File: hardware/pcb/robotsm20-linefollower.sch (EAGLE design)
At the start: 132 parts, among them Q5 BSS138LT3G, Q6 BSS138LT3G, Q7 BSS138LT3G, Q8 BSS138LT3G, U1 STM32F405RG

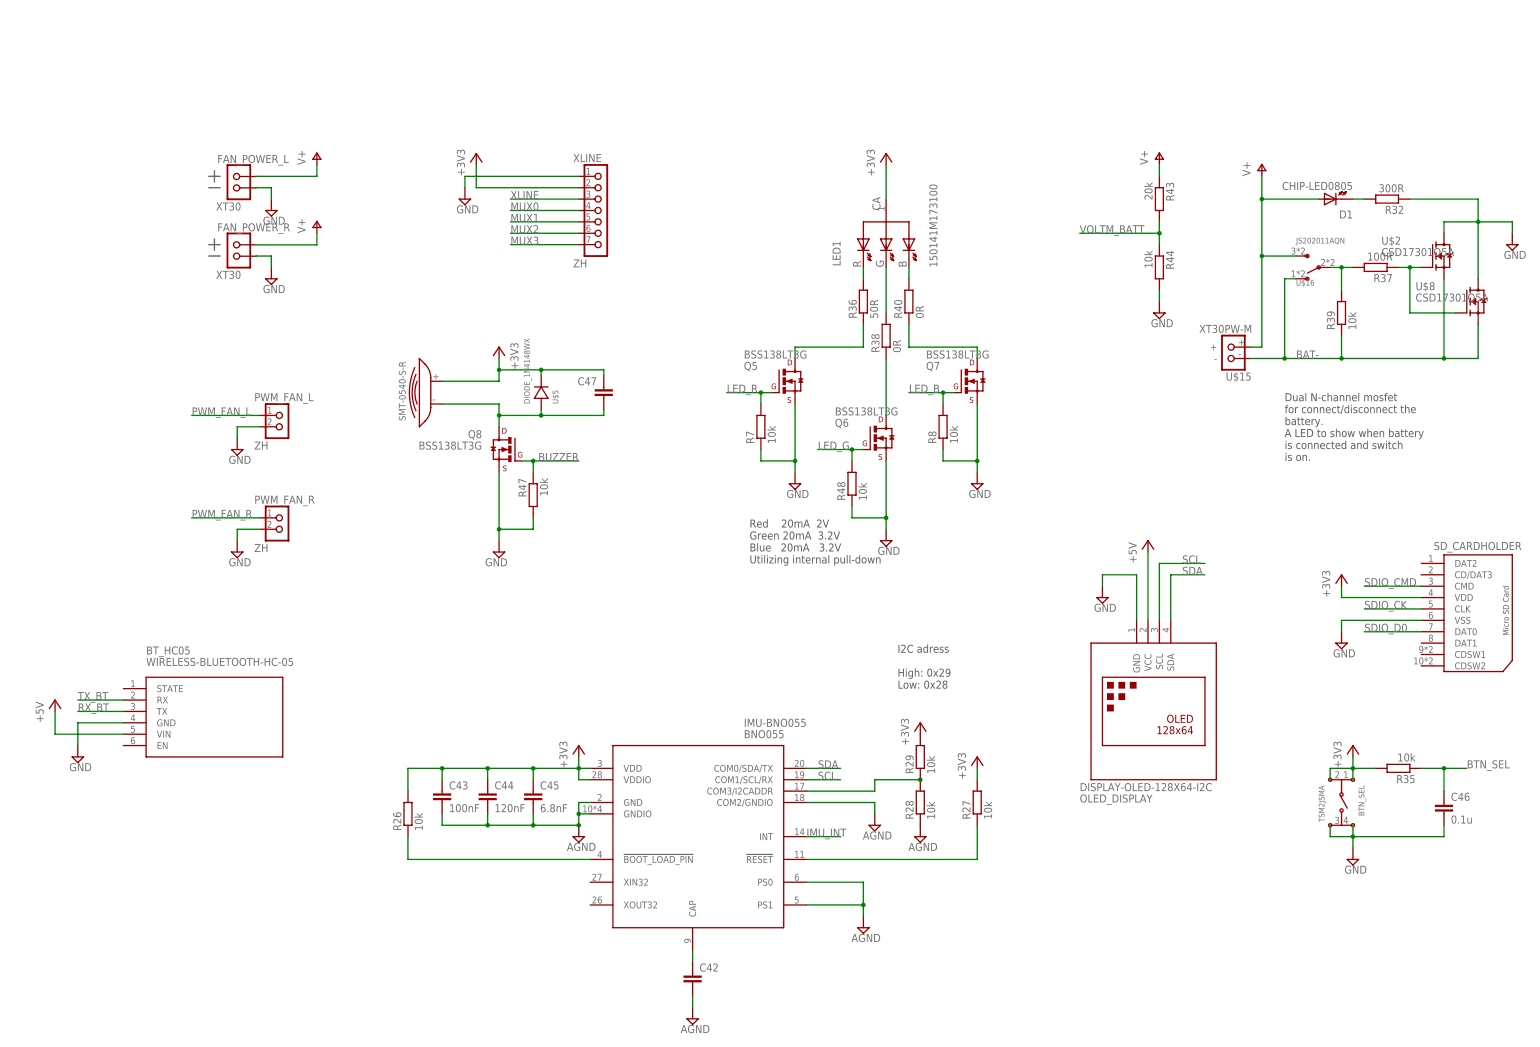
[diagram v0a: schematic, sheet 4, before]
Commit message: Motor mounts added
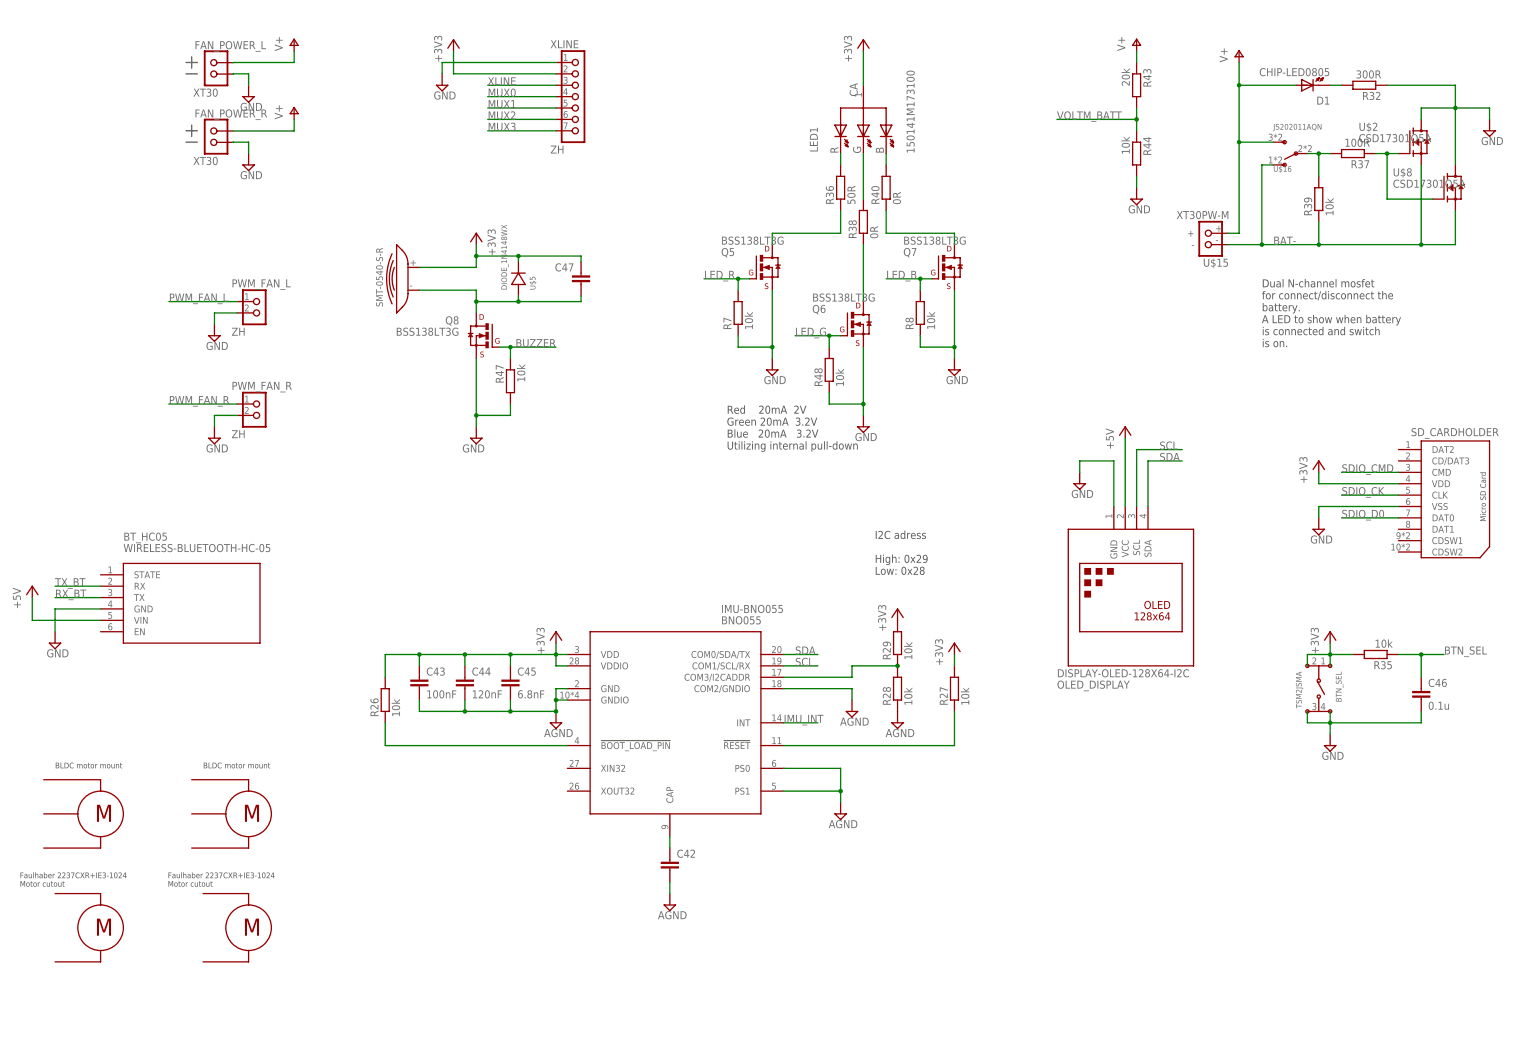
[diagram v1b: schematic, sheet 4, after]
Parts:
- added U$11, U$12: FAULHABER-2237CXR+IE3-1024, MISC:FAULHABER-2237CXR+IE3-1024
- added U$6, U$7: EMAX-1306/1606_MOTOR_MOUNT, MISC:EMAX-1306/1606_MOTOR_MOUNT
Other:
- moved on the sheet: BTN_SEL, BT_HC05, C42, C43, C44, C45, C46, C47, D1, FAN_POWER_L, FAN_POWER_R, IMU-BNO055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

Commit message: Correction work
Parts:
- removed C41: 270pF, rcl:C-EUC0805
- removed R16, R21: (no value), rcl:R-EU_R0603
- added COSC: 270pF, rcl:C-EUC0805
- added CVCC: 0.1µF, rcl:C-EUC0805
- added ROSC: 3.14k, rcl:R-EU_R0603
- added TP1, TP2: TEST-POINT3X5, Isaks Bibliotek:TEST-POINT3X5
- ENC_L, ENC_R: value ZR_B6B-ZR -> ZH-6
- MOTOR_L, MOTOR_R: value EH_B2B-EH -> EH-2
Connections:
- removed net N$24: BOOST.EN, R16.1
- removed net N$29: C41.1, MOTORDRIVER.VCC, R21.2, R23.2
- removed net N$9: C3.1, CURRENTAMP.VS
- new net VCC5V: CVCC.1, MOTORDRIVER.TBLKAB, MOTORDRIVER.VCC, R1.2, R2.2, R23.2, ROSC.2
- net +3V3: now also C3.1, CURRENTAMP.VS; no longer R1.2, R2.2
- net GND: now also COSC.2, CVCC.2; no longer C41.2
- net LO1: now also TP2.1
- net LO2: now also TP1.1
- net N$31: now also COSC.1, ROSC.1; no longer R21.1
- net V+: no longer R16.2
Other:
- note added: "Float to enable IC"
- note added: "Vref for constant current mode Iout = Vref * 2.5"
- note added: "fchop = 1/4 Rosc^(-0.8) f in MHz, R in Kohm 1.8kohm for 150kHz 3.14ohm for 100kHz 8.2kohm for 50kHz"
- moved on the sheet: R3

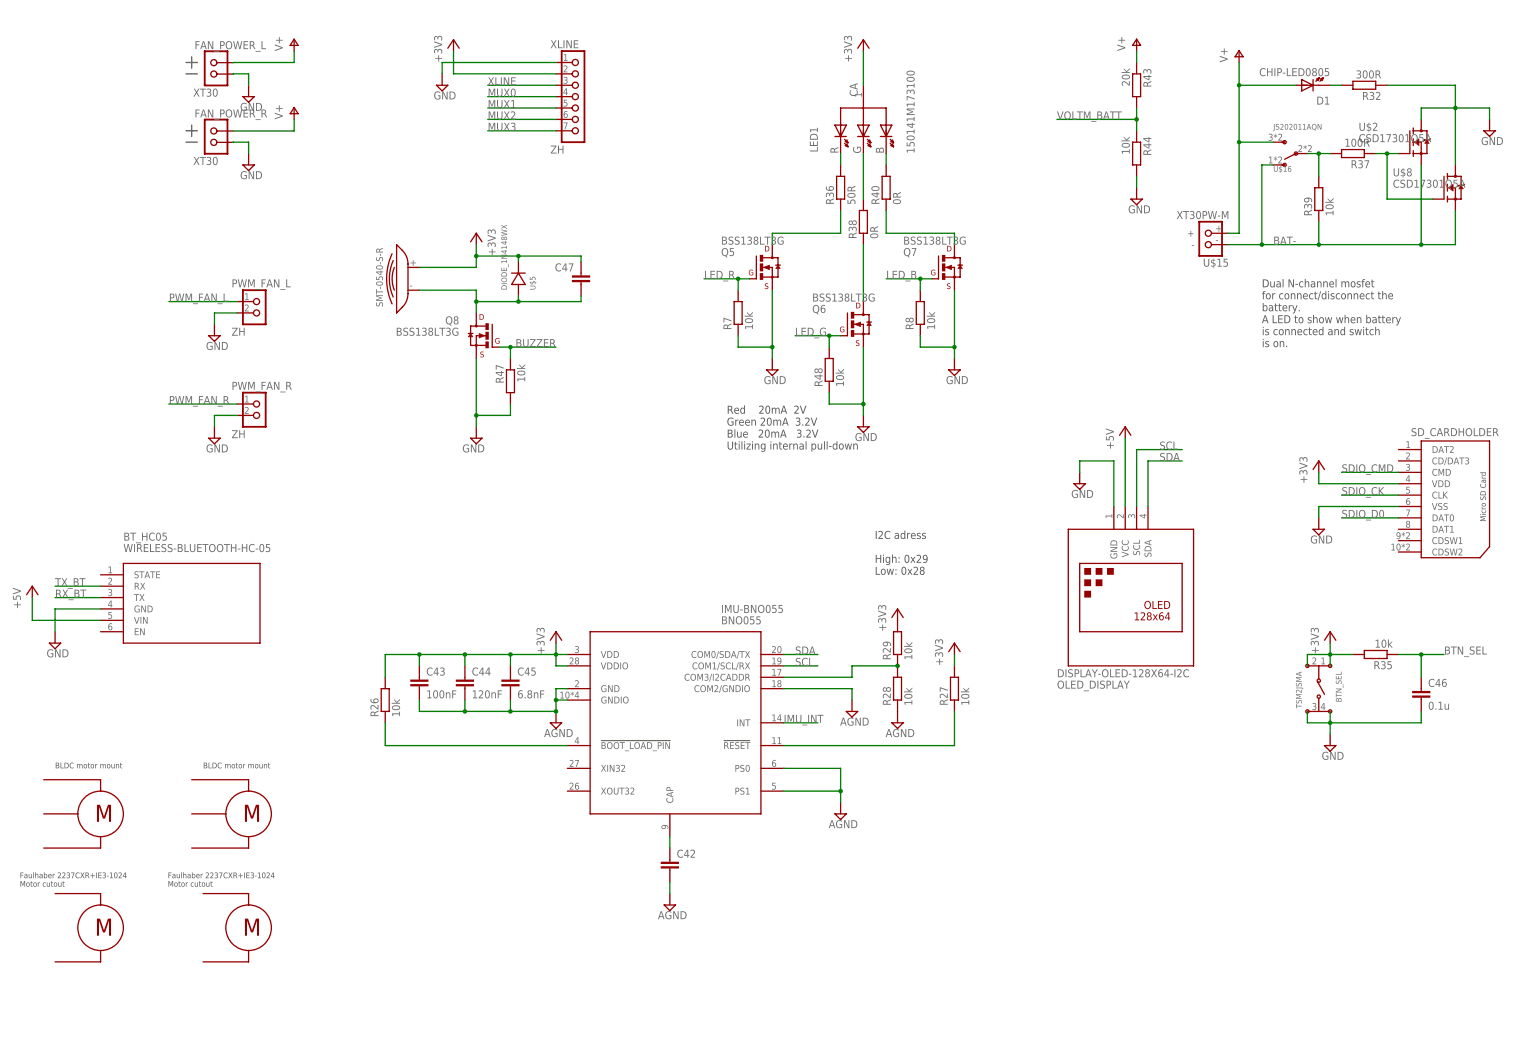
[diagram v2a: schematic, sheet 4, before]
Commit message: Checked schematic towards datasheets
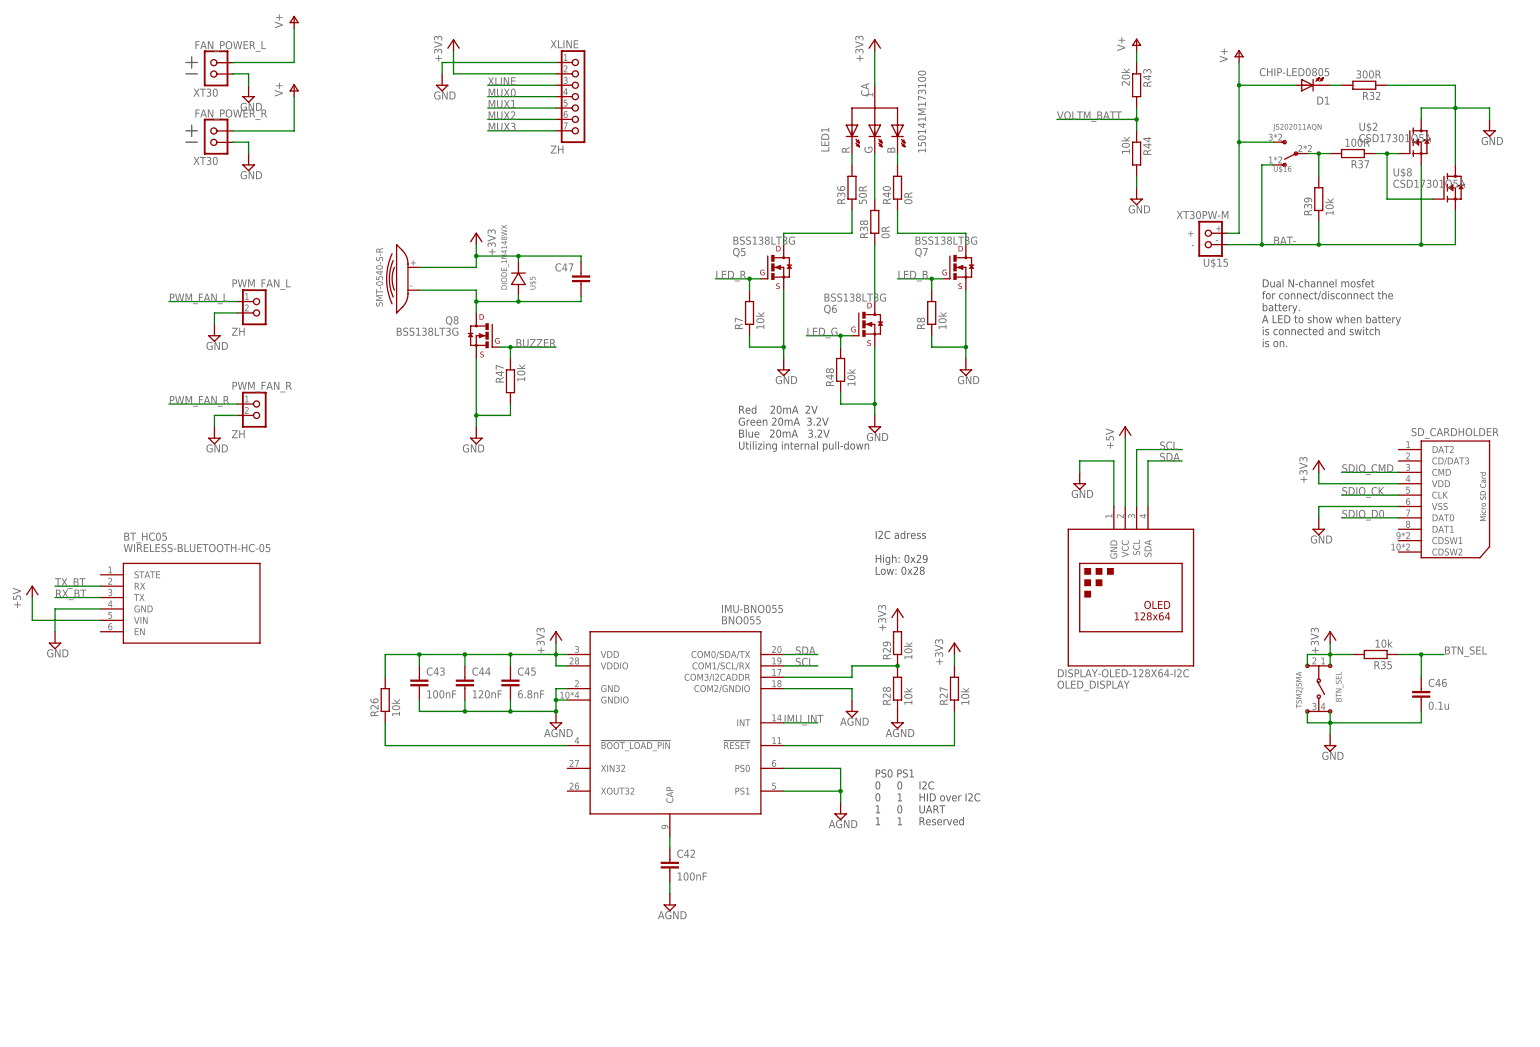
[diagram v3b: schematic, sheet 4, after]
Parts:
- removed U$11, U$12: FAULHABER-2237CXR+IE3-1024, MISC:FAULHABER-2237CXR+IE3-1024
- removed U$6, U$7: EMAX-1306/1606_MOTOR_MOUNT, MISC:EMAX-1306/1606_MOTOR_MOUNT
- added C13: 0.1µF, rcl:C-EUC0805
- added C14: 4.7µF, rcl:C-EUC0805
- C19: value (none) -> 1.5nF
- C20: value (none) -> 110pF
- C21: value 0.1µF -> 100nF
- C42: value (none) -> 100nF
- R10: value (none) -> 15.4k
- R14, R15: value (none) -> 10R
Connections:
- new net N$2: BOOST.VCC, C14.1
- net GND: now also C13.2, C14.2
- net V+: now also C13.1
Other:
- note added: "PS0 PS1 0 0 I2C 0 1 HID over I2C 1 0 UART 1 1 Reserved"
- moved on the sheet: C21, LED1, Q5, Q6, Q7, R36, R38, R40, R48, R7, R8

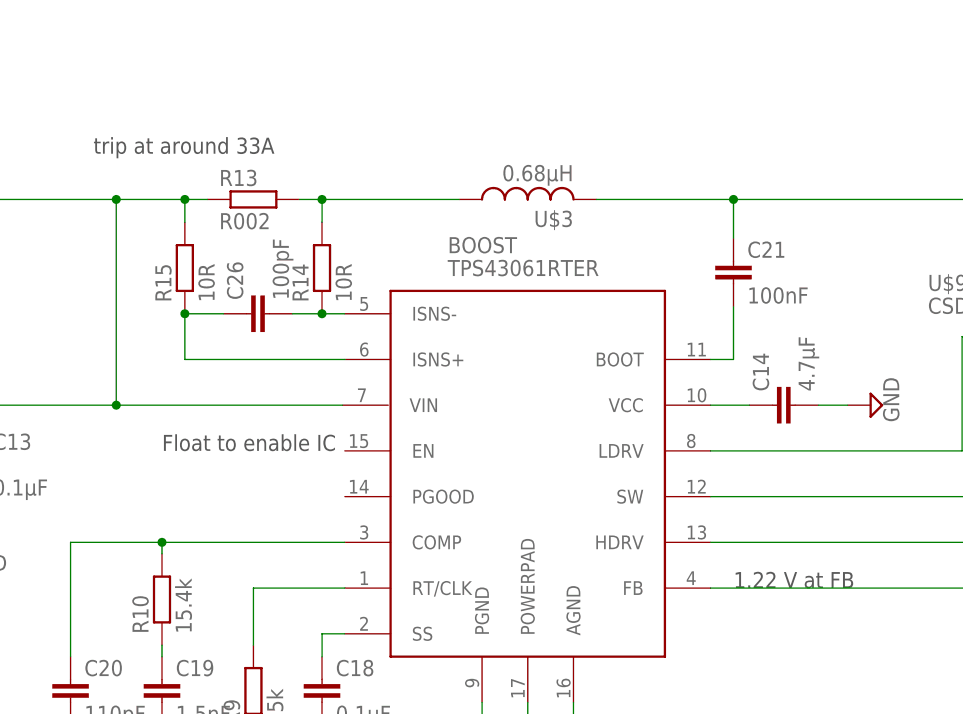
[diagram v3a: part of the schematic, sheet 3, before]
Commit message: Moved parts together for boost in board
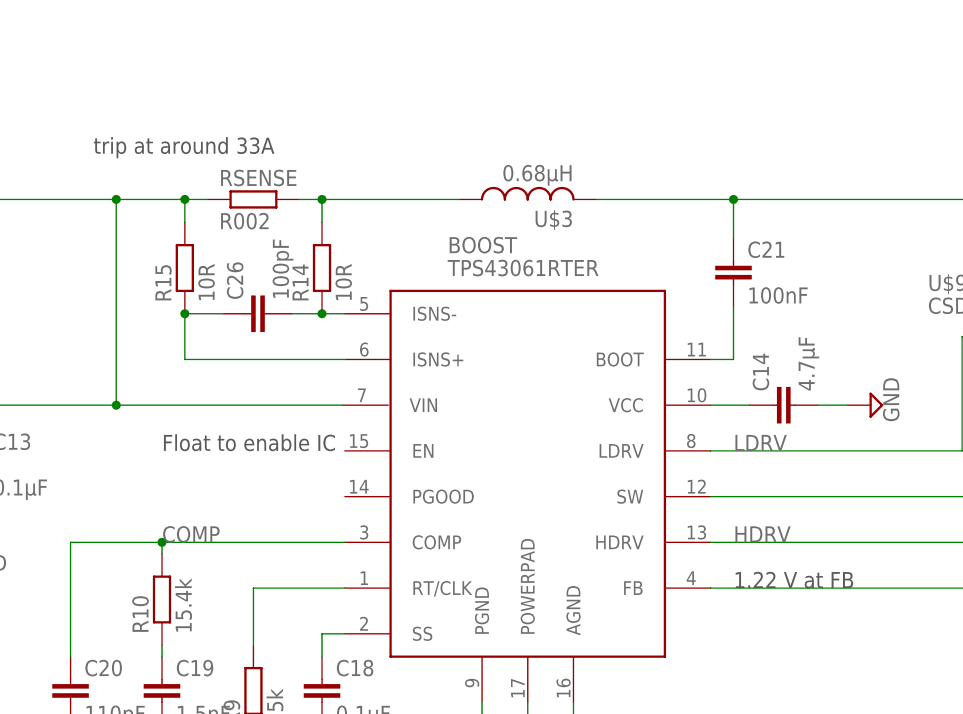
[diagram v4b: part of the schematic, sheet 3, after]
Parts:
- removed R13: R002, rcl:R-EU_R1206W
- added RSENSE: R002, rcl:R-EU_R2512W
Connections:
- net N$1 renamed HDRV
- net N$14 renamed COMP
- net N$17 renamed LDRV
- net N$18: now also RSENSE.2; no longer R13.2
- net V+: now also RSENSE.1; no longer R13.1
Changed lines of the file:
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@@
 <part name="R12" library="rcl" library_urn="urn:adsk.eagle:library:334" deviceset="R-EU_" device="R0603" package3d_urn="urn:adsk.eagle:package:23555/3" value="88k"/>
 <part name="SUPPLY32" library="supply2" library_urn="urn:adsk.eagle:library:372" deviceset="GND" device=""/>
-<part name="R13" library="rcl" library_urn="urn:adsk.eagle:library:334" deviceset="R-EU_" device="R1206W" package3d_urn="urn:adsk.eagle:package:23539/2" value="R002"/>
 <part name="C22" library="rcl" library_urn="urn:adsk.eagle:library:334" deviceset="C-EU" device="C0805" package3d_urn="urn:adsk.eagle:package:23617/2" value="22µF"/>
 <part name="C23" library="rcl" library_urn="urn:adsk.eagle:library:334" deviceset="C-EU" device="C0805" package3d_urn="urn:adsk.eagle:package:23617/2" value="22µF"/>
@@
 <part name="C14" library="rcl" library_urn="urn:adsk.eagle:library:334" deviceset="C-EU" device="C0805" package3d_urn="urn:adsk.eagle:package:23617/2" value="4.7µF"/>
 <part name="SUPPLY22" library="supply2" library_urn="urn:adsk.eagle:library:372" deviceset="GND" device=""/>
+<part name="RSENSE" library="rcl" library_urn="urn:adsk.eagle:library:334" deviceset="R-EU_" device="R2512W" package3d_urn="urn:adsk.eagle:package:23565/2" value="R002"/>
 </parts>
 <sheets>
@@
 <attribute name="VALUE" x="79.375" y="-66.675" size="1.778" layer="96"/>
 </instance>
-<instance part="R13" gate="G$1" x="-35.56" y="-2.54" smashed="yes" grouprefs="BOOST-12V">
-<attribute name="NAME" x="-39.37" y="-1.0414" size="1.778" layer="95"/>
-<attribute name="VALUE" x="-39.37" y="-5.842" size="1.778" layer="96"/>
-</instance>
 <instance part="C22" gate="G$1" x="106.68" y="-7.874" smashed="yes" grouprefs="BOOST-12V">
 <attribute name="NAME" x="108.204" y="-7.493" size="1.778" layer="95"/>
@@
 <instance part="SUPPLY22" gate="GND" x="33.02" y="-25.4" smashed="yes" rot="R90">
 <attribute name="VALUE" x="36.195" y="-27.305" size="1.778" layer="96" rot="R90"/>
+</instance>
+<instance part="RSENSE" gate="G$1" x="-35.56" y="-2.54" smashed="yes">
+<attribute name="NAME" x="-39.37" y="-1.0414" size="1.778" layer="95"/>
+<attribute name="VALUE" x="-39.37" y="-5.842" size="1.778" layer="96"/>
 </instance>
 </instances>
@@
 <pinref part="BOOST" gate="G$1" pin="VIN"/>
 <wire x1="-25.654" y1="-25.4" x2="-50.8" y2="-25.4" width="0.1524" layer="91" grouprefs="BOOST-12V"/>
-<pinref part="R13" gate="G$1" pin="1"/>
 <pinref part="R15" gate="G$1" pin="2"/>
 <wire x1="-50.8" y1="-25.4" x2="-50.8" y2="-2.54" width="0.1524" layer="91" grouprefs="BOOST-12V"/>
@@
 <wire x1="-66.04" y1="-25.4" x2="-50.8" y2="-25.4" width="0.1524" layer="91"/>
 <junction x="-50.8" y="-25.4"/>
+<pinref part="RSENSE" gate="G$1" pin="1"/>
 </segment>
 </net>
@@
 </segment>
 </net>
-<net name="N$14" class="0">
+<net name="COMP" class="0">
 <segment>
 <pinref part="BOOST" gate="G$1" pin="COMP"/>
@@
 <wire x1="-55.88" y1="-40.64" x2="-45.72" y2="-40.64" width="0.1524" layer="91" grouprefs="BOOST-12V"/>
 <junction x="-45.72" y="-40.64" grouprefs="BOOST-12V"/>
+<label x="-45.72" y="-40.64" size="1.778" layer="95"/>
 </segment>
 </net>
@@
 </segment>
 </net>
-<net name="N$17" class="0">
+<net name="LDRV" class="0">
 <segment>
 <pinref part="BOOST" gate="G$1" pin="LDRV"/>
@@
 <wire x1="43.18" y1="-17.78" x2="48.26" y2="-17.78" width="0.1524" layer="91" grouprefs="BOOST-12V"/>
 <pinref part="U$9" gate="G$1" pin="G"/>
+<label x="17.78" y="-30.48" size="1.778" layer="95"/>
 </segment>
 </net>
@@
 <segment>
 <pinref part="U$3" gate="G$1" pin="1"/>
-<pinref part="R13" gate="G$1" pin="2"/>
 <wire x1="-12.7" y1="-2.54" x2="-27.94" y2="-2.54" width="0.1524" layer="91" grouprefs="BOOST-12V"/>
 <pinref part="R14" gate="G$1" pin="2"/>
@@
 <wire x1="-27.94" y1="-5.08" x2="-27.94" y2="-2.54" width="0.1524" layer="91" grouprefs="BOOST-12V"/>
 <junction x="-27.94" y="-2.54" grouprefs="BOOST-12V"/>
+<pinref part="RSENSE" gate="G$1" pin="2"/>
 </segment>
 </net>
@@
 </segment>
 </net>
-<net name="N$1" class="0">
+<net name="HDRV" class="0">
 <segment>
 <pinref part="BOOST" gate="G$1" pin="HDRV"/>
@@
 <pinref part="U$10" gate="G$1" pin="G"/>
 <wire x1="68.58" y1="-40.64" x2="68.58" y2="-7.62" width="0.1524" layer="91"/>
-</segment>
-</net>
+<label x="17.78" y="-40.64" size="1.778" layer="95"/>
+</segment>
+</net>
